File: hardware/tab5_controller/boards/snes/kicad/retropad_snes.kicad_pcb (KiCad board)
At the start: 2 copper layers, 125 x 55 mm, 29 parts, among them J1 Tab5 Ext.Port1, J2 UPDI, SW1 UP, SW10 START, SW11 MENU, SW12 L, SW13 R, SW2 DOWN, SW3 LEFT, SW4 RIGHT, SW5 X, SW6 B, SW7 Y, SW8 A, SW9 SELECT, U1 AVR32DD28-I/SO

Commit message: Tab5 controller boards: back-side references as board text for EasyEDA
EasyEDA's KiCad import drew the references of R1-R3, R6-R9 and C1-C3
mirrored top to bottom on the back silkscreen, while board-level mirrored
text (ID0-ID3, UPDI labels, board name) came through correctly. Each back
footprint's reference is now redrawn as board text at the same place,
size and angle KiCad shows, and the footprint's own reference is hidden.
KiCad renders are unchanged; DRC counts are unchanged.

Co-Authored-By: Claude Opus 5.5 (1M context) <noreply@anthropic.com>
Claude-Session: https://claude.ai/code/session_01TRQq2EkHCDXMenNyd2D33U
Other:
- board text added: "C1"
- board text added: "C2"
- board text added: "C3"
- board text added: "C4"
- board text added: "J2"
- board text added: "R1"
- board text added: "R2"
- board text added: "R3"
- board text added: "R6"
- board text added: "R7"
- board text added: "R8"
- board text added: "R9"
- board text added: "U1"
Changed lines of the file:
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@@
     (property "Sheetname" "")
     (attr smd)
-    (fp_text reference "R3" (at 0 1.65 90) (layer "B.SilkS")
+    (fp_text reference "R3" (at 0 1.65 90) (layer "B.SilkS") hide
         (effects (font (size 1 1) (thickness 0.15)) (justify mirror))
     )
@@
     (property "Sheetname" "")
     (attr smd exclude_from_bom)
-    (fp_text reference "R9" (at 0 1.65 90) (layer "B.SilkS")
+    (fp_text reference "R9" (at 0 1.65 90) (layer "B.SilkS") hide
         (effects (font (size 1 1) (thickness 0.15)) (justify mirror))
     )
@@
     (property "Sheetname" "")
     (attr smd)
-    (fp_text reference "C1" (at 0 1.68 90) (layer "B.SilkS")
+    (fp_text reference "C1" (at 0 1.68 90) (layer "B.SilkS") hide
         (effects (font (size 1 1) (thickness 0.15)) (justify mirror))
     )
@@
     (property "Sheetname" "")
     (attr smd exclude_from_bom)
-    (fp_text reference "R8" (at 0 1.65 90) (layer "B.SilkS")
+    (fp_text reference "R8" (at 0 1.65 90) (layer "B.SilkS") hide
         (effects (font (size 1 1) (thickness 0.15)) (justify mirror))
     )
@@
     (property "Sheetname" "")
     (attr smd)
-    (fp_text reference "R6" (at 0 1.65 90) (layer "B.SilkS")
+    (fp_text reference "R6" (at 0 1.65 90) (layer "B.SilkS") hide
         (effects (font (size 1 1) (thickness 0.15)) (justify mirror))
     )
@@
     (property "Sheetname" "")
     (attr smd)
-    (fp_text reference "C2" (at 0 1.68) (layer "B.SilkS")
+    (fp_text reference "C2" (at 0 1.68) (layer "B.SilkS") hide
         (effects (font (size 1 1) (thickness 0.15)) (justify mirror))
     )
@@
     (property "Sheetname" "")
     (attr through_hole)
-    (fp_text reference "J2" (at 0 2.33 90) (layer "B.SilkS")
+    (fp_text reference "J2" (at 0 2.33 90) (layer "B.SilkS") hide
         (effects (font (size 1 1) (thickness 0.15)) (justify mirror))
     )
@@
     (property "Sheetname" "")
     (attr smd)
-    (fp_text reference "U1" (at 0 9.9 90) (layer "B.SilkS")
+    (fp_text reference "U1" (at 0 9.9 90) (layer "B.SilkS") hide
         (effects (font (size 1 1) (thickness 0.15)) (justify mirror))
     )
@@
     (property "Sheetname" "")
     (attr smd)
-    (fp_text reference "R1" (at 0 1.65 90) (layer "B.SilkS")
+    (fp_text reference "R1" (at 0 1.65 90) (layer "B.SilkS") hide
         (effects (font (size 1 1) (thickness 0.15)) (justify mirror))
     )
@@
     (property "Sheetname" "")
     (attr smd)
-    (fp_text reference "R7" (at 0 1.65 90) (layer "B.SilkS")
+    (fp_text reference "R7" (at 0 1.65 90) (layer "B.SilkS") hide
         (effects (font (size 1 1) (thickness 0.15)) (justify mirror))
     )
@@
     (property "Sheetname" "")
     (attr smd)
-    (fp_text reference "C3" (at 0 1.68) (layer "B.SilkS")
+    (fp_text reference "C3" (at 0 1.68) (layer "B.SilkS") hide
         (effects (font (size 1 1) (thickness 0.15)) (justify mirror))
     )
@@
     (property "Sheetname" "")
     (attr smd)
-    (fp_text reference "C4" (at 0 1.68 90) (layer "B.SilkS")
+    (fp_text reference "C4" (at 0 1.68 90) (layer "B.SilkS") hide
         (effects (font (size 1 1) (thickness 0.15)) (justify mirror))
     )
@@
     (property "Sheetname" "")
     (attr smd)
-    (fp_text reference "R2" (at 0 1.65 90) (layer "B.SilkS")
+    (fp_text reference "R2" (at 0 1.65 90) (layer "B.SilkS") hide
         (effects (font (size 1 1) (thickness 0.15)) (justify mirror))
     )
@@
   (gr_line (start 165 94) (end 165 83.5)
     (stroke (width 0.1) (type default)) (layer "Edge.Cuts"))
+  (gr_text "R2" (at 85.65 93 90) (layer "B.SilkS")
+    (effects (font (size 1 1) (thickness 0.15)) (justify mirror))
+  )
+  (gr_text "J2" (at 132.33 86.5 90) (layer "B.SilkS")
+    (effects (font (size 1 1) (thickness 0.15)) (justify mirror))
+  )
+  (gr_text "R8" (at 128.65 99 90) (layer "B.SilkS")
+    (effects (font (size 1 1) (thickness 0.15)) (justify mirror))
+  )
+  (gr_text "C4" (at 117.68 90.5 90) (layer "B.SilkS")
+    (effects (font (size 1 1) (thickness 0.15)) (justify mirror))
+  )
+  (gr_text "C1" (at 93.68 96 90) (layer "B.SilkS")
+    (effects (font (size 1 1) (thickness 0.15)) (justify mirror))
+  )
+  (gr_text "C2" (at 102.1 84.02) (layer "B.SilkS")
+    (effects (font (size 1 1) (thickness 0.15)) (justify mirror))
+  )
   (gr_text "ID0" (at 121 102.2) (layer "B.SilkS")
     (effects (font (size 0.8 0.8) (thickness 0.12)) (justify mirror))
   )
+  (gr_text "U1" (at 113.9 93.5 90) (layer "B.SilkS")
+    (effects (font (size 1 1) (thickness 0.15)) (justify mirror))
+  )
   (gr_text "ID3" (at 130 102.2) (layer "B.SilkS")
     (effects (font (size 0.8 0.8) (thickness 0.12)) (justify mirror))
   )
+  (gr_text "R7" (at 125.65 99 90) (layer "B.SilkS")
+    (effects (font (size 1 1) (thickness 0.15)) (justify mirror))
+  )
+  (gr_text "C3" (at 106 99.92) (layer "B.SilkS")
+    (effects (font (size 1 1) (thickness 0.15)) (justify mirror))
+  )
+  (gr_text "R6" (at 122.65 99 90) (layer "B.SilkS")
+    (effects (font (size 1 1) (thickness 0.15)) (justify mirror))
+  )
+  (gr_text "R9" (at 131.65 99 90) (layer "B.SilkS")
+    (effects (font (size 1 1) (thickness 0.15)) (justify mirror))
+  )
+  (gr_text "R3" (at 99.25 85.7 90) (layer "B.SilkS")
+    (effects (font (size 1 1) (thickness 0.15)) (justify mirror))
+  )
   (gr_text "RetroPad SNES rev 0.1" (at 140 86.5) (layer "B.SilkS")
     (effects (font (size 1 1) (thickness 0.15)) (justify mirror))
@@
     (effects (font (size 0.8 0.8) (thickness 0.12)) (justify mirror))
   )
+  (gr_text "R1" (at 87.65 93 90) (layer "B.SilkS")
+    (effects (font (size 1 1) (thickness 0.15)) (justify mirror))
+  )
   (gr_text "VERIFY PIN 1 vs KEYBOARD" (at 66 95.4) (layer "F.SilkS")

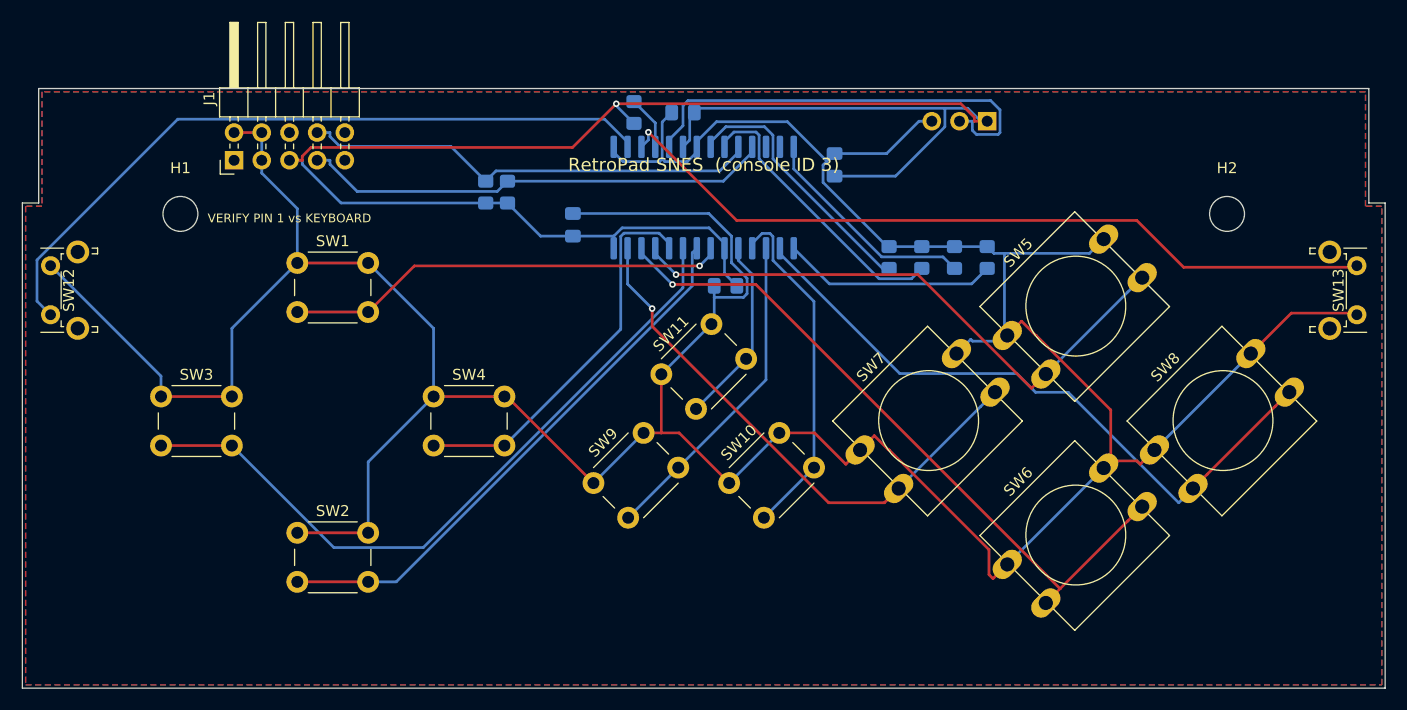
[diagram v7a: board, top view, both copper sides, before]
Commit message: Tab5 controller boards: anchor every footprint on its pad centre for EasyEDA
EasyEDA's KiCad import shifts a footprint whose anchor is off its centre by
the anchor-to-centre distance. On the Genesis board this put the 12 mm
switches on H2 and on R6-R9; J1, J2 and the 6 mm switches were shifted
too. Every footprint now has its anchor on the centre of its pads, in the
routed boards and in the RetroPad switch library, with all pads, tracks
and drawings where they were (checked pad by pad; DRC and netlist
unchanged). --back-refs-only becomes --easyeda-fixups, which applies both
EasyEDA changes to a routed board.

Co-Authored-By: Claude Opus 5.5 (1M context) <noreply@anthropic.com>
Claude-Session: https://claude.ai/code/session_01TRQq2EkHCDXMenNyd2D33U
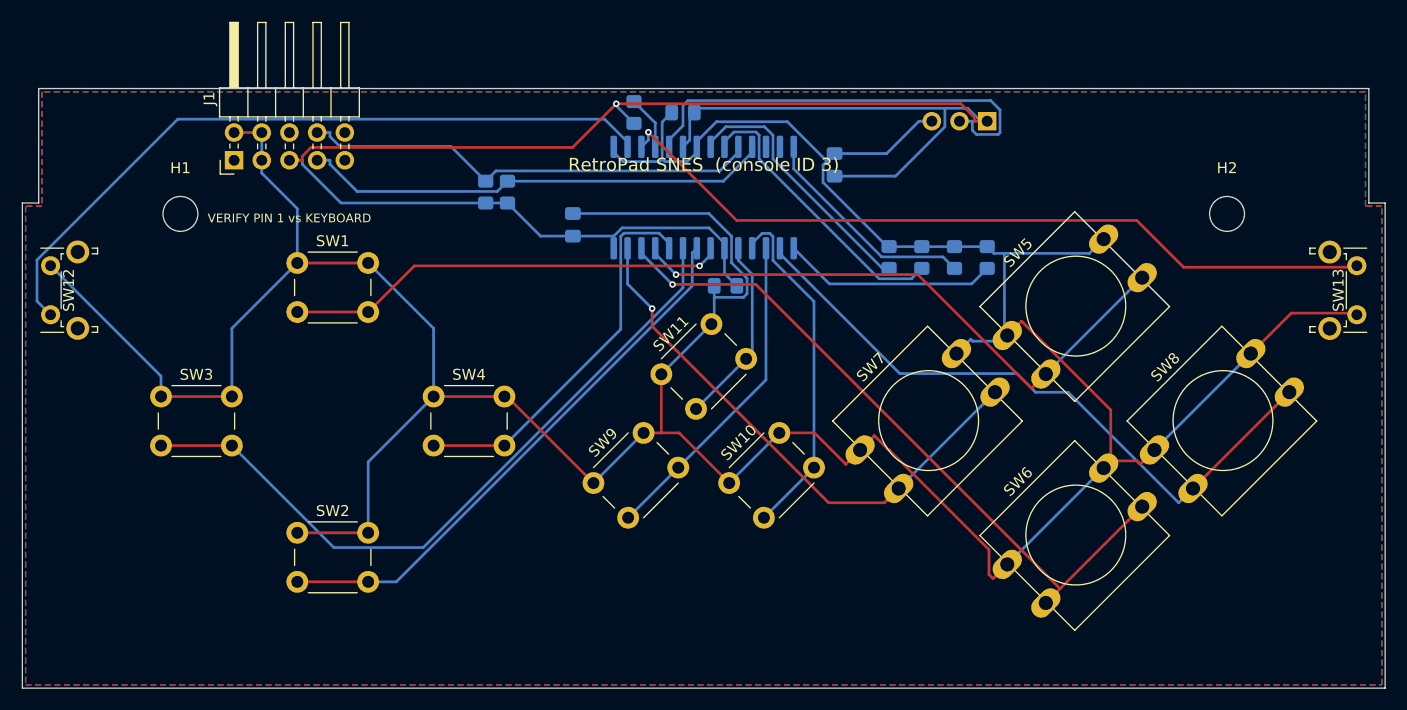
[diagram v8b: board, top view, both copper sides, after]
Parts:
- moved SW5 6.73 mm to (138.0, 103.5)
- moved SW6 6.73 mm to (138.0, 124.5)
- moved SW7 6.73 mm to (124.5, 114.0)
- moved SW8 6.73 mm to (151.5, 114.0)
- moved J1 5.24 mm to (66.0, 88.8)
- moved SW1 3.95 mm to (70.0, 101.8)
- moved SW2 3.95 mm to (70.0, 126.5)
- moved SW3 3.95 mm to (57.5, 114.0)
- moved SW4 3.95 mm to (82.5, 114.0)
- moved SW11 3.95 mm to (104.0, 109.0)
- moved SW9 3.95 mm to (97.8, 119.0)
- moved SW10 3.95 mm to (110.2, 119.0)
- moved J2 2.54 mm to (127.5, 86.5)
- moved SW12 2.25 mm to (44.1, 102.0)
- moved SW13 2.25 mm to (163.9, 102.0)
